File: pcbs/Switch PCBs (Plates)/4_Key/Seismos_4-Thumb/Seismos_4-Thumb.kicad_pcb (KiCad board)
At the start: 2 copper layers, 38 x 48.4 mm, 12 parts, among them J1 SM10B-SRSS-TB(LF)(SN), SW1 Switch_SK6812-E_Diode, SW2 Switch_SK6812-E_Diode, SW3 Switch_SK6812-E_Diode, SW4 Switch_SK6812-E_Diode

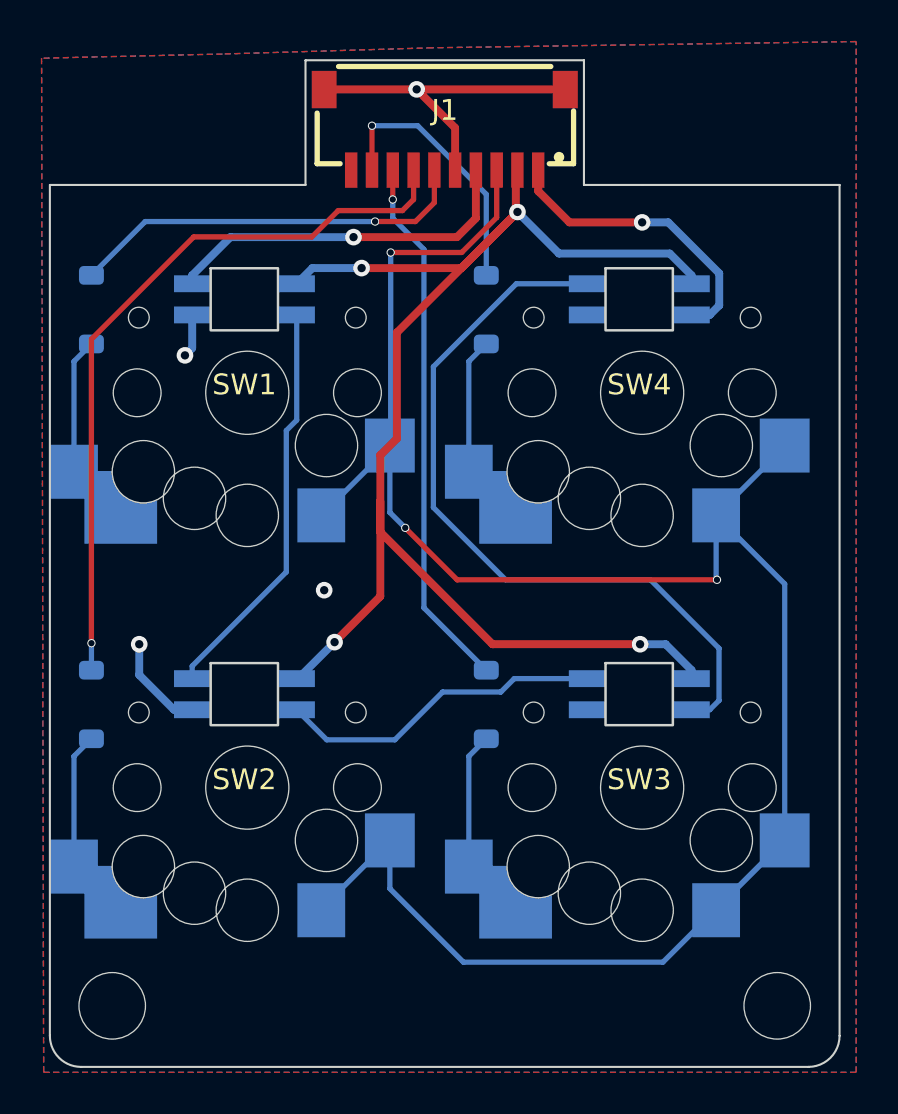
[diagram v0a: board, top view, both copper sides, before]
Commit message: Added stencils for new and old PCBs
Created stencils for solder pasting PCBs with the core and plates.
I ordered both new and old versions so two stencils were made; however,
the holes for the old variant are misaligned. For this, use the other
aligning holes.

In addition, repaired footprints for switches where the switch footprint
was appearing on the reverse side. This is now fixed.
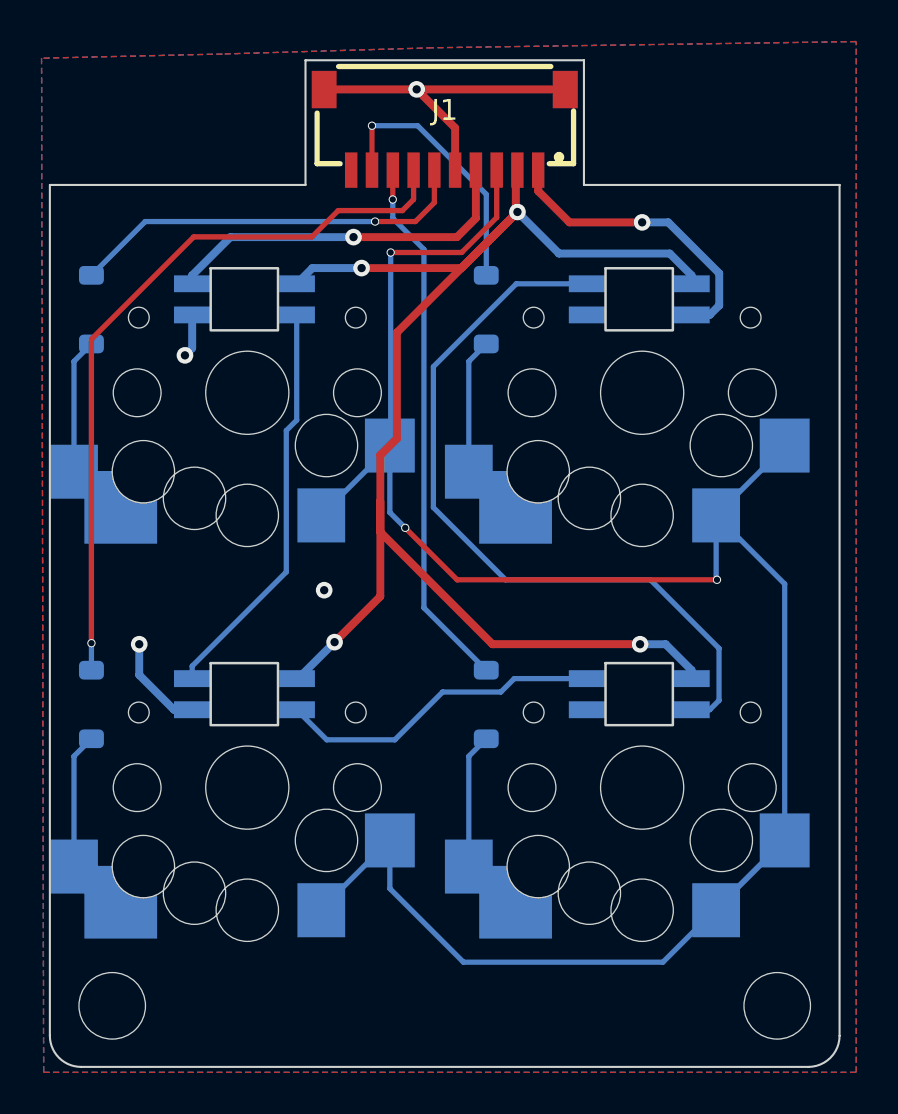
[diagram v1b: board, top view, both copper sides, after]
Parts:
- SW1, SW2, SW3, SW4: moved to B.Cu
- turned SW1 to 180 degrees
- turned SW2 to 180 degrees
- turned SW3 to 180 degrees
- turned SW4 to 180 degrees

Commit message: Release v1.1
***NOTE***: If you have a previous commit, please update your files.
This commit fixes the incorrect RGB pinout and power switch as the
RGB footprint was incorrect.
The power switch behaviour is also fixed in this commit so the position
matches on both sides.
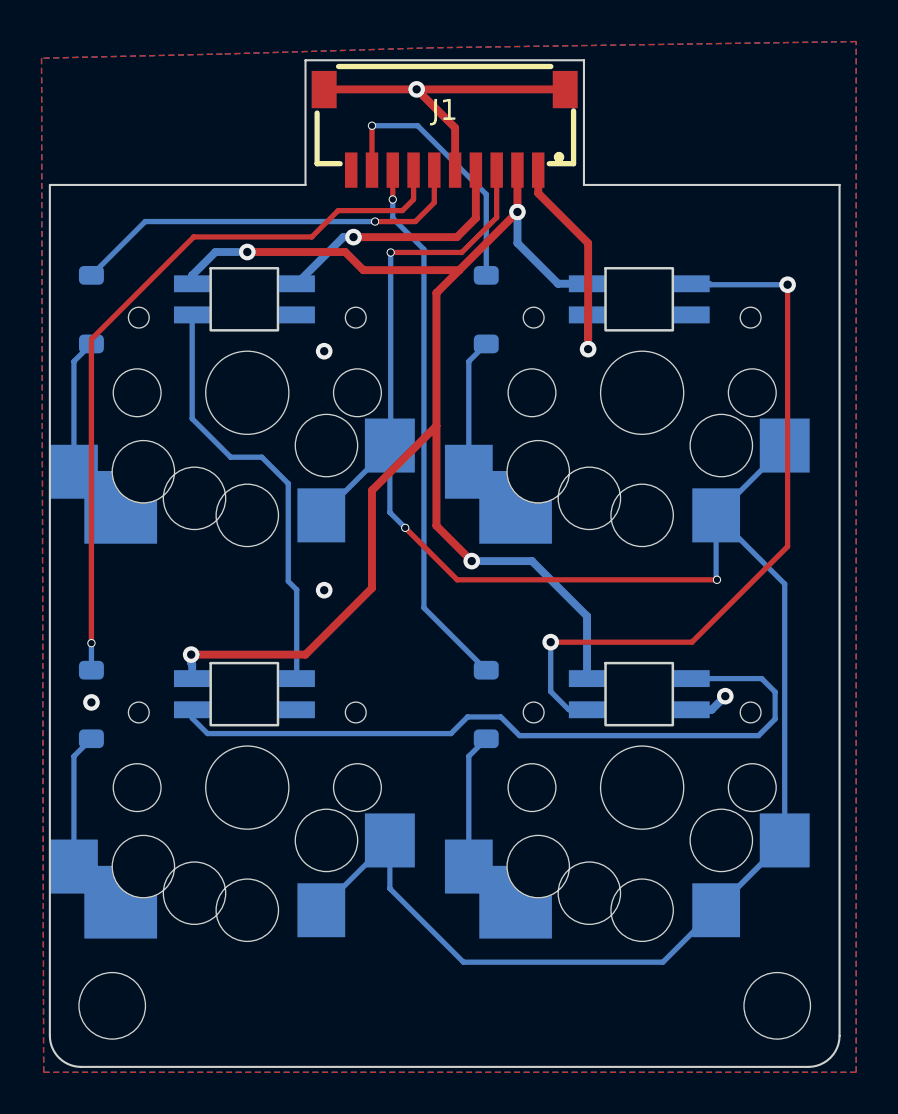
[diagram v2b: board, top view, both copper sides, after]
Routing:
- net Net-(SW2B-DOUT): track 15.8 -> 35.4 mm
- net /RGB_In: track 17.5 -> 12.2 mm
- net GND: track 22.1 -> 17.1 mm, vias 4 -> 5
- net /RGB_Out: track 14.4 -> 11.3 mm
- net Net-(SW3B-DOUT): track 36.4 -> 35.0 mm, vias 0 -> 2
- net Net-(SW1B-DOUT): track 19.6 -> 20.5 mm
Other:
- board text added: "Rev. 1.1"
- board text removed: "Rev. 1.0"
